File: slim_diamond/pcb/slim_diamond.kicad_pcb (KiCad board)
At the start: 2 copper layers, 87.6 x 92.3 mm, 25 parts, among them J1 JST PH 2.0 battery, SW1 pinky, SW10 index_bottom, SW11 thumb_outer, SW12 thumb_inner, SW13 MSK-12C02, SW2 ring_top, SW3 ring_home, SW4 ring_bottom, SW5 middle_top, SW6 middle_home, SW7 middle_bottom, SW8 index_top, SW9 index_home, U1 XIAO nRF52840

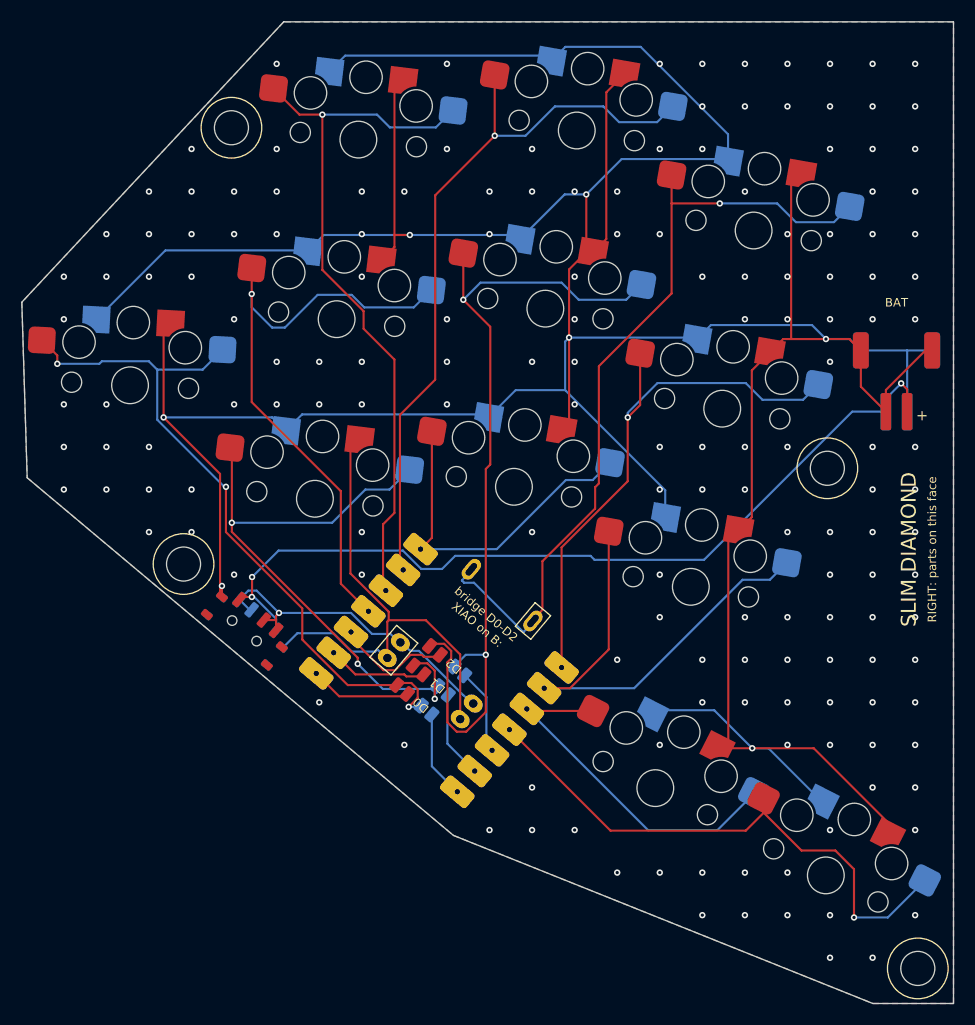
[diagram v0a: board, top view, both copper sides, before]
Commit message: Add a top plate and a solid base to the Slim Diamond
The plate covers the whole board. It's a 1.2 mm Choc v1 plate sitting 1.0 mm over
the PCB, with 14.0 mm cutouts (13.8 mm plus cut_tol per side). A 0.5 mm pocket in
its underside clears the solder around the Xiao, support pillars stand on the PCB,
and countersunk bosses take M3 x 8 flat-head screws. The screws go through the
plate and PCB into the base, and the plate prints top face down.

The base is now solid up to the PCB, with a pocket per part and 0.6 mm of
clearance, so the board rests on plastic everywhere: stiffer and quieter. The
bottom edges of the case and plate get a 45-degree chamfer for the cut-stone
look.

The JST socket moves so its plug has room: the battery was flush against the
opening. The Xiao renders were wrong: flipping the footprint moved its pads off
their tracks and turned the USB end around. Now only the 3D models are turned
over, and the Xiao stand-in looks like the real module. The fit check covers the
plate, the solder blobs, the screws and the magnets. The pin map is unchanged.

Co-Authored-By: Claude Opus 5.5 <noreply@anthropic.com>
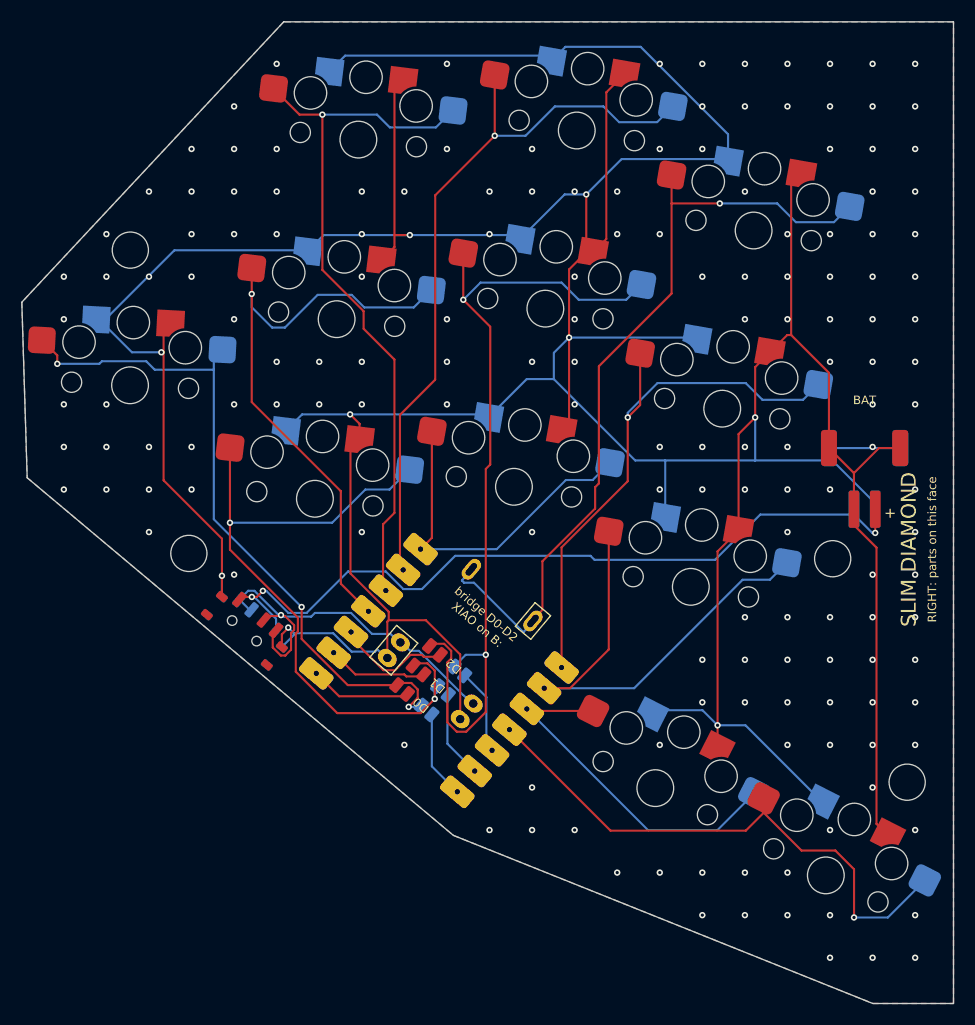
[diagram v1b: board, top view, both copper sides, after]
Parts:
- moved H4 61.0 mm to (127.0, 123.5)
- moved H3 60.5 mm to (66.5, 123.0)
- moved H1 17.5 mm to (134.0, 144.5)
- moved H2 14.9 mm to (61.0, 94.5)
- moved J1 9.65 mm to (130.0, 116.0)
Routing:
- net GND: track 471.4 -> 493.1 mm, vias 171 -> 170
- net VBAT: track 31.0 -> 38.5 mm
- net BAT+: track 81.3 -> 74.1 mm
- net K_ring_bottom: track 58.6 -> 64.3 mm, vias 3 -> 2
- net K_pinky: track 66.8 -> 65.2 mm

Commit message: Fix the Slim Diamond's USB-C, power switch and PCB fit for printing
A review of the board and case found four things the fit check didn't
cover:

- USB-C: the port sat 3.6 mm behind the outer wall, in a 10 x 4.4 mm
  hole, so a cable's overmold stopped about 3 mm short of seating. The
  wall now has a recess the size of the largest Type-C overmold
  (13 x 7 mm) from the receptacle's face out.
- The PCB's edge ran 0.86 mm past the receptacle, where a thick
  overmold reaches above the PCB's underside. The board edge is now
  notched in front of the port, and the board is rerouted (DRC clean,
  same pin map).
- The power switch's lever reached 0.45 mm into the wall, so the PCB
  couldn't drop straight in, and its tip sat 2.3 mm deep in a 5 x 2.8 mm
  hole. It now has a slot open to the top that the lever slides down,
  widening outwards for a fingernail.
- The PCB and plate had 0.3 mm to the walls, less than JLCPCB's outline
  tolerance plus a printed wall's shrink. The outer walls now sit 0.5 mm
  off (the seam stays at 0.3).

check_fit.py now also checks a plugged-in USB-C cable against the case
and the PCB, and the lever's path as the PCB drops in. Against the old
design they read 120, 1.9 and 4.4 mm3. fab.sh writes the JLCPCB zip, and
render.sh now also makes BUILD.md's Xiao close-ups.

Co-Authored-By: Claude Opus 5.5 <noreply@anthropic.com>
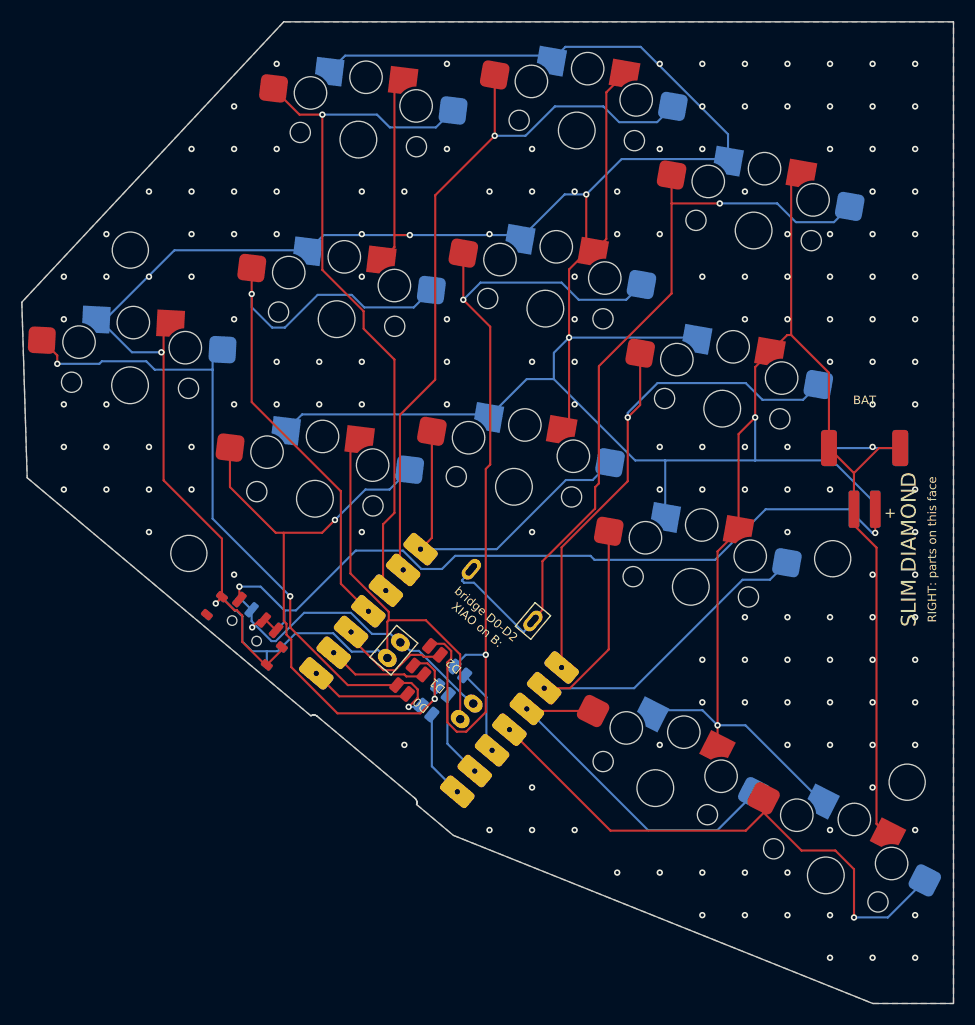
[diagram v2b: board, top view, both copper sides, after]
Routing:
- net GND: track 493.1 -> 508.4 mm, vias 170 -> 168
- net VBAT: track 38.5 -> 32.0 mm
- net K_ring_bottom: track 64.3 -> 59.9 mm
- net BAT+: track 74.1 -> 73.2 mm, vias 3 -> 2
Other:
- outline, holes or cut-outs redrawn

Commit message: Add a reset button to the Slim Diamond, reachable through the plate
A 5.1 x 5.1 x 2.0 mm SMD tact switch (XKB TS-1187A-B-D-B, pads after
KiCad's SW_SPST_TL3342) on the switch face, in the nook between the index
column's bottom key and the thumbs, 7.65 mm from the nearest keycap. It
reboots a closed half, and a double press enters the bootloader, which the
Xiao's own button (facing the case floor) can't once the case is assembled.

- Wiring: the Xiao's reset test pad (Seeed pad 17, "EN" in their symbol;
  TP2 on P0.18/RESET in their schematic) through a plated hole filled from
  the switch face, like VBAT/GND/NFC1, boxed on the silkscreen. Pads 17 and
  18 mirror onto each other, so each mount's hole lands under the other
  mount's GND pad: each hole gets its own net (RST_L, RST_R) wired only to
  its half's button, and the grounded one only grounds the unused copy.
- Plate: a pocket over the body and collar up to 1.5 mm over the PCB, then
  a 45-degree cone (2.8 mm throat, 4.2 mm at the top) that prints top face
  down without support. The plunger ends 0.2 mm under the plate's top.
- check_fit: button vs plate, plunger column open, plunger depth, reset
  hole blobs vs plate, cone vs keycaps; ALL CLEAR. DRC clean (all
  severities), 0 unconnected; pinout.json unchanged.
- Renders, BOM, BUILD and README updated.

Co-Authored-By: Claude Opus 5.5 <noreply@anthropic.com>
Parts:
- added SW14: TS-1187A reset, slim_diamond:SW_TS1187A_Reversible, F.Cu at (129.5, 137.0)
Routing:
- net RST_L: track 0.00 -> 50.5 mm
- net RST_R: track 0.00 -> 49.0 mm, vias 0 -> 1
- net K_middle_home: track 80.4 -> 62.7 mm
- net GND: track 508.4 -> 507.8 mm, vias 168 -> 169

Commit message: Make one Slim Diamond board for both the XIAO and the Super52840
The two boards become one. The modules differ only under the battery,
the 12th key and the USB-C legs; their edge pins, reset pad and firmware
are the same.

- Battery: one small fill hole per pad spot (BATM, nearer the middle;
  BATU, nearer the USB end), inside both modules' pads and 0.25 mm clear
  of the Super52840's GPIO row under the other half's module. The pads
  are swapped between the modules, so a selector on the switch face picks
  which hole is +: two rows of solder jumpers, labelled by what they do,
  +MID (the XIAO) and +USB (the Super52840). It sits inside the module
  outline, clear of both modules' pads and the switch housings, under
  the plate's solder pocket.
- P0.09: a hole under each module's pad, on one net. Under a XIAO, the
  Super52840's hole touches NFC2 (P0.10, unused and idle).
- The clearance holes under the Super52840's USB-C legs stay, fenced
  off from the router.

The XIAO/Super52840 MODULE switch, pcb_super52840/ and its fab zip are
gone. Severity-all DRC: no violations, 0 unconnected. The pin map is
unchanged. A contact check of every bare pad under the module, for both
modules in both mounts, finds every intended joint and only the known
harmless extras. The build guide sets the selector in step 1, and checks
before any battery goes in that VBAT doesn't beep to GND, which catches
a wrong or doubled row.

Co-Authored-By: Claude Opus 5.5 <noreply@anthropic.com>
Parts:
- added JS1: +MID BATM, slim_diamond:SolderJumper_F, F.Cu at (93.8, 131.7)
- added JS2: +MID BATU, slim_diamond:SolderJumper_F, F.Cu at (91.6, 129.9)
- added JS3: +MID BATM, slim_diamond:SolderJumper_B, F.Cu at (91.6, 129.9)
- added JS4: +MID BATU, slim_diamond:SolderJumper_B, F.Cu at (93.8, 131.7)
- added JS5: +USB BATM, slim_diamond:SolderJumper_F, F.Cu at (95.2, 130.0)
- added JS6: +USB BATU, slim_diamond:SolderJumper_F, F.Cu at (93.0, 128.2)
- added JS7: +USB BATM, slim_diamond:SolderJumper_B, F.Cu at (93.0, 128.2)
- added JS8: +USB BATU, slim_diamond:SolderJumper_B, F.Cu at (95.2, 130.0)
- U1: value XIAO nRF52840 -> XIAO nRF52840 / Super52840; footprint slim_diamond:XIAO_nRF52840_Reversible -> slim_diamond:nRF52840_Module_Reversible
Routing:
- net GND: track 507.8 -> 560.0 mm, vias 169 -> 173
- net BATU: track 0.00 -> 25.0 mm, vias 0 -> 1
- net BATM: track 0.00 -> 21.7 mm
- net K_ring_bottom: track 59.9 -> 47.3 mm, vias 2 -> 3
- net RST_R: track 49.0 -> 59.3 mm, vias 1 -> 0
- net K_index_bottom: track 46.4 -> 38.0 mm, vias 0 -> 1
- net X_L13: track 8.25 -> 14.9 mm, vias 0 -> 1
- net K_index_top: track 75.9 -> 82.5 mm
- net VBAT: track 32.0 -> 38.1 mm, vias 1 -> 2
- net BAT+: track 73.2 -> 77.9 mm, vias 2 -> 3
- net RST_L: track 50.5 -> 54.9 mm, vias 0 -> 1
- net X_L14: track 8.25 -> 12.6 mm
- net X_L1: track 9.51 -> 12.1 mm
- net K_middle_home: track 62.7 -> 61.1 mm
- net K_pinky: track 65.1 -> 63.9 mm
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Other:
- board text added: "+MID"
- board text added: "+USB"

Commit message: Correct the Super52840 leg clearance and P0.09 hole from a second photo
A photo beside a ruler, measured against the 2.54 mm pin pitch like the
first, agrees on the battery pads (within 0.1 mm) but places the USB-C leg
slots at y -4.76 and -8.94. The first estimate, -4.0 and -8.8, was read
by eye and had the inner pair 0.8 mm off. Detected the same way in both
photos, the slots measure about 0.7 x 2.0 mm, so the clearance holes are
now 1.2 x 2.6 mm on them. The GPIO row sits at x 5.06 or 5.3 depending
on the photo, so the P0.09 hole moves to 5.2, inside the pad either way.

The larger holes left 4 connections unrouted at 0.15 mm clearance;
0.14 (JLCPCB's minimum is 0.127) routes completely, and is now the
default. Severity-all DRC: clean, 0 unconnected. The pin map is
unchanged. The contact check passes for both modules in both mounts,
with the GPIO row at either photo's position.

Co-Authored-By: Claude Opus 5.5 <noreply@anthropic.com>
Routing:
- net K_pinky: track 63.9 -> 108.5 mm
- net GND: track 560.0 -> 541.3 mm, vias 173 -> 165
- net K_ring_bottom: track 47.3 -> 59.0 mm, vias 3 -> 2
- net RST_R: track 59.3 -> 50.0 mm, vias 0 -> 1
- net K_index_bottom: track 38.0 -> 46.3 mm, vias 1 -> 0
- net X_L13: track 14.9 -> 8.29 mm, vias 1 -> 0
- net X_L1: track 12.1 -> 17.3 mm, vias 0 -> 1
- net BAT+: track 77.9 -> 73.4 mm, vias 3 -> 2
- net BATU: track 25.0 -> 28.3 mm, vias 1 -> 3
- net K_ring_home: track 58.1 -> 54.9 mm
- net BATM: track 21.7 -> 24.9 mm, vias 0 -> 1
- net VBAT: track 38.1 -> 41.1 mm, vias 2 -> 4
- net RST_L: track 54.9 -> 56.4 mm, vias 1 -> 2
- net X_L14: track 12.6 -> 11.1 mm
- net X_L3: track 9.67 -> 11.1 mm
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
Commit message: Allow for the Super52840's off-centre USB-C
More photos of the Super52840, one straight top-down with a ruler
(21.75 px/mm, matching the pin pitch), show its USB-C 0.3 to 0.6 mm off
centre, towards the D0..D6 pins. The leg slots in the earlier photos are
off centre the same way. The halves are mirrored, so the offset flips
between them, and everything around the port now allows for it either way:
- Leg clearance holes are 1.6 mm wide (were 1.2), covering the legs at x
  -4.65 and +4.05 in both halves.
- The notch in the PCB edge is 14.2 mm (was 13.0), and the case's recess
  14.6 mm (was 13.4).
- check_fit plugs in a full-size cable centred and 0.6 mm off either
  way: all 0 mm3.

A third reading of the GPIO row, from the board edge and the
castellations, puts it at x 5.2, where the P0.09 hole already is.

Routed at 0.14 mm clearance. Severity-all DRC: clean, 0 unconnected. The
pin map is unchanged. The contact check passes for both modules in both
mounts, with the GPIO row at all three readings and the legs wholly
inside their holes.

Co-Authored-By: Claude Opus 5.5 <noreply@anthropic.com>
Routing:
- net K_pinky: track 108.5 -> 77.0 mm, vias 3 -> 4
- net X_L14: track 11.1 -> 23.4 mm, vias 0 -> 2
- net K_ring_bottom: track 59.0 -> 47.2 mm
- net RST_R: track 50.0 -> 56.5 mm
- net GND: track 541.3 -> 536.3 mm, vias 165 -> 169
- net VBAT: track 41.1 -> 43.3 mm, vias 4 -> 3
- net X_L3: track 11.1 -> 9.42 mm, vias 0 -> 1
- net RST_L: track 56.4 -> 54.8 mm, vias 2 -> 3
- net BATM: track 24.9 -> 23.6 mm, vias 1 -> 0
- net BATU: track 28.3 -> 27.1 mm, vias 3 -> 4
- net K_middle_home: track 60.9 -> 61.6 mm
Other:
- outline, holes or cut-outs redrawn
